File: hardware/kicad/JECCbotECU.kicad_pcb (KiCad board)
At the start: 2 copper layers, 100 x 60 mm, 70 parts, among them CN1 ADAFRUIT_FEATHER, CN2 691382010004, CN3 691382010005, CN4 691382010004, P1 USB_B, P2 CONN_02X05, P3 CONN_02X03, P4 CONN_02X05, P5 WR-TBL_691313710002, U1 STM32F103C8Tx, U2 BSS138, U3 BSS138, U4 BNO055, U5 TPS54335A, U6 GAPTEC_6S8W4_1.6RP, U7 LT1117, Y1 Crystal_Small

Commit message: bugfix
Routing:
- net +3V3: track 336.1 -> 330.5 mm
- net GND: vias 62 -> 63
- net +5V: vias 10 -> 7
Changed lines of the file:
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@@
     (thickness 1.6)
     (drawings 4)
-    (tracks 869)
+    (tracks 866)
     (zones 0)
     (modules 70)
@@
   (via (at 181.60492 61.33592) (size 0.8) (drill 0.4) (layers F.Cu B.Cu) (net 1))
   (via (at 142.70228 60.0964) (size 0.8) (drill 0.4) (layers F.Cu B.Cu) (net 1))
-  (via (at 147.39112 60.33008) (size 0.8) (drill 0.4) (layers F.Cu B.Cu) (net 1))
+  (via (at 146.66468 60.03544) (size 0.8) (drill 0.4) (layers F.Cu B.Cu) (net 1))
   (via (at 150.749 59.93892) (size 0.8) (drill 0.4) (layers F.Cu B.Cu) (net 1))
   (via (at 148.48332 43.84548) (size 0.8) (drill 0.4) (layers F.Cu B.Cu) (net 1))
@@
   (via (at 131.37388 47.36084) (size 0.8) (drill 0.4) (layers F.Cu B.Cu) (net 1))
   (via (at 128.40716 54.39156) (size 0.8) (drill 0.4) (layers F.Cu B.Cu) (net 1))
-  (via (at 144.10944 53.53304) (size 0.8) (drill 0.4) (layers F.Cu B.Cu) (net 1))
   (via (at 125.47092 55.03164) (size 0.8) (drill 0.4) (layers F.Cu B.Cu) (net 1))
   (via (at 130.28676 56.20512) (size 0.8) (drill 0.4) (layers F.Cu B.Cu) (net 1))
@@
   (via (at 151.11476 83.97748) (size 0.8) (drill 0.4) (layers F.Cu B.Cu) (net 1))
   (via (at 167.80256 86.97976) (size 0.8) (drill 0.4) (layers F.Cu B.Cu) (net 1))
+  (via (at 155.80868 57.72404) (size 0.8) (drill 0.4) (layers F.Cu B.Cu) (net 1))
+  (via (at 188.18352 46.66488) (size 0.8) (drill 0.4) (layers F.Cu B.Cu) (net 1))
   (segment (start 167.088 67.1) (end 165.64 67.1) (width 0.25) (layer F.Cu) (net 2))
   (segment (start 167.628 66.56) (end 167.088 67.1) (width 0.25) (layer F.Cu) (net 2))
@@
   (segment (start 169.4046 66.41916) (end 170.50512 65.31864) (width 1) (layer F.Cu) (net 2))
   (segment (start 170.53052 49.53508) (end 175.38592 49.54524) (width 1) (layer F.Cu) (net 2))
-  (segment (start 158.23 60.335) (end 157.42752 59.53252) (width 0.25) (layer F.Cu) (net 2))
-  (via (at 154.85364 59.5122) (size 0.8) (drill 0.4) (layers F.Cu B.Cu) (net 2))
-  (segment (start 157.42752 59.53252) (end 154.87396 59.53252) (width 0.25) (layer F.Cu) (net 2))
-  (segment (start 154.87396 59.53252) (end 154.85364 59.5122) (width 0.25) (layer F.Cu) (net 2))
-  (segment (start 155.419325 59.5122) (end 155.429485 59.50204) (width 0.25) (layer B.Cu) (net 2))
-  (segment (start 154.85364 59.5122) (end 155.419325 59.5122) (width 1) (layer B.Cu) (net 2))
-  (segment (start 155.429485 59.50204) (end 159.37484 59.50204) (width 1) (layer B.Cu) (net 2))
   (segment (start 159.37484 59.50204) (end 161.47288 57.404) (width 1) (layer B.Cu) (net 2))
   (segment (start 161.47288 57.404) (end 161.47288 56.0832) (width 1) (layer B.Cu) (net 2))
@@
   (segment (start 164.084 77.99) (end 165.0492 77.98816) (width 0.5) (layer F.Cu) (net 2))
   (segment (start 165.0492 77.98816) (end 166.70344 77.99) (width 0.5) (layer F.Cu) (net 2))
+  (segment (start 158.23 60.335) (end 158.23 60.32824) (width 0.25) (layer F.Cu) (net 2))
+  (via (at 157.61716 59.7154) (size 0.8) (drill 0.4) (layers F.Cu B.Cu) (net 2))
+  (segment (start 158.23 60.32824) (end 157.61716 59.7154) (width 0.25) (layer F.Cu) (net 2))
+  (segment (start 158.396205 59.50204) (end 159.37484 59.50204) (width 1) (layer B.Cu) (net 2))
+  (segment (start 158.182845 59.7154) (end 158.396205 59.50204) (width 1) (layer B.Cu) (net 2))
+  (segment (start 157.61716 59.7154) (end 158.182845 59.7154) (width 1) (layer B.Cu) (net 2))
   (segment (start 162.04 65.5) (end 162.04 60.96) (width 0.25) (layer F.Cu) (net 3))
   (segment (start 163.73094 58.211466) (end 163.73094 57.15) (width 0.25) (layer F.Cu) (net 3))
@@
   (segment (start 177.2666 46.4312) (end 177.30216 46.39564) (width 0.25) (layer B.Cu) (net 12))
   (segment (start 176.10836 46.39564) (end 177.292 46.39564) (width 1) (layer B.Cu) (net 12))
-  (via (at 154.813 53.21808) (size 0.8) (drill 0.4) (layers F.Cu B.Cu) (net 12))
-  (via (at 149.49932 56.1086) (size 0.8) (drill 0.4) (layers F.Cu B.Cu) (net 12))
-  (via (at 153.24836 56.73344) (size 0.8) (drill 0.4) (layers F.Cu B.Cu) (net 12))
   (via (at 142.20952 64.96812) (size 0.8) (drill 0.4) (layers F.Cu B.Cu) (net 13))
   (segment (start 142.20952 65.517882) (end 142.20952 64.96812) (width 0.25) (layer F.Cu) (net 13))
@@
   (segment (start 144.81048 47.95012) (end 145.4658 47.2948) (width 0.25) (layer F.Cu) (net 69))
   (zone (net 33) (net_name VBAT) (layer F.Cu) (hatch edge 0.508)
+    (priority 1)
     (connect_pads (clearance 0.508))
     (min_thickness 0.254)
@@
   )
   (zone (net 7) (net_name +12V) (layer F.Cu) (hatch edge 0.508)
+    (priority 1)
     (connect_pads (clearance 0.508))
     (min_thickness 0.254)
@@
   )
   (zone (net 11) (net_name /power/REG_5V_PH) (layer F.Cu) (hatch edge 0.508)
+    (priority 1)
     (connect_pads (clearance 0.508))
     (min_thickness 0.254)
@@
   )
   (zone (net 12) (net_name +5V) (layer F.Cu) (hatch edge 0.508)
+    (priority 1)
     (connect_pads (clearance 0.508))
     (min_thickness 0.254)
@@
     (polygon
       (pts
-        (xy 152.27808 52.50688) (xy 152.273 58.02376) (xy 151.60244 58.70956) (xy 144.62252 58.69432) (xy 144.02816 57.80024)
-        (xy 144.03832 52.21224) (xy 144.99336 51.83632) (xy 151.92756 51.83632)
-      )
-    )
-  )
-  (zone (net 12) (net_name +5V) (layer F.Cu) (hatch edge 0.508)
-    (connect_pads (clearance 0.508))
-    (min_thickness 0.254)
-    (fill yes (arc_segments 32) (thermal_gap 0.508) (thermal_bridge_width 0.508))
-    (polygon
-      (pts
-        (xy 157.26156 47.1932) (xy 157.38856 58.20664) (xy 156.6164 58.74512) (xy 151.384 58.74512) (xy 152.03932 53.15204)
-        (xy 151.82088 51.98364) (xy 151.83612 47.41164) (xy 152.33904 46.86808) (xy 153.20772 46.84776) (xy 156.8958 46.8122)
+        (xy 157.26156 47.1932) (xy 157.25648 53.9242) (xy 156.48432 54.46268) (xy 151.384 58.74512) (xy 151.388221 58.709092)
+        (xy 144.62252 58.69432) (xy 144.02816 57.80024) (xy 144.03832 52.21224) (xy 144.99336 51.83632) (xy 151.821371 51.83632)
+        (xy 151.83612 47.41164) (xy 152.33904 46.86808) (xy 153.20772 46.84776) (xy 156.8958 46.8122)
       )
     )
@@
       )
     )
+  )
+  (zone (net 1) (net_name GND) (layer B.Cu) (hatch edge 0.508)
+    (priority 1)
+    (connect_pads (clearance 0.508))
+    (min_thickness 0.254)
+    (fill yes (arc_segments 32) (thermal_gap 0.508) (thermal_bridge_width 0.508))
+    (polygon
+      (pts
+        (xy 189.96152 40.05072) (xy 190.02756 100.1776) (xy 89.87536 100.44176) (xy 89.97696 40.005)
+      )
+    )

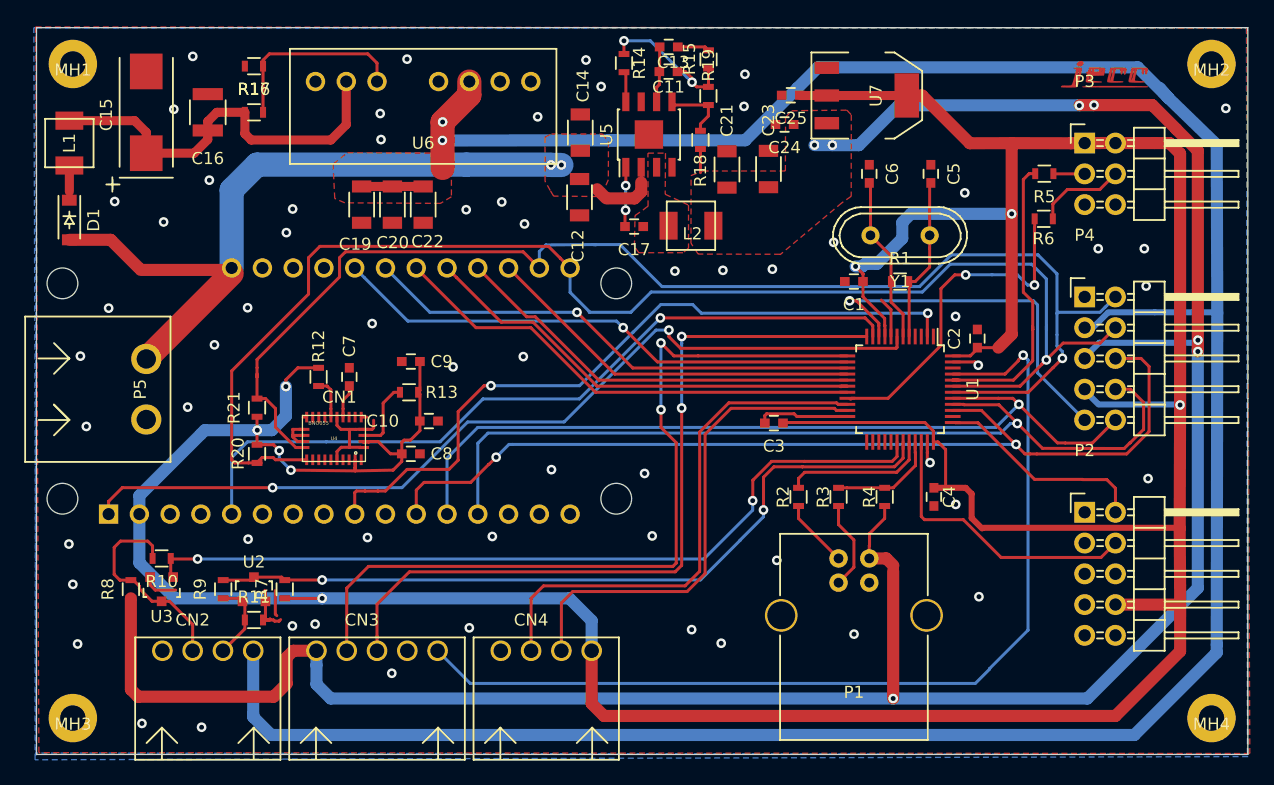
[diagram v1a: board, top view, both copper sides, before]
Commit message: silkscreen design
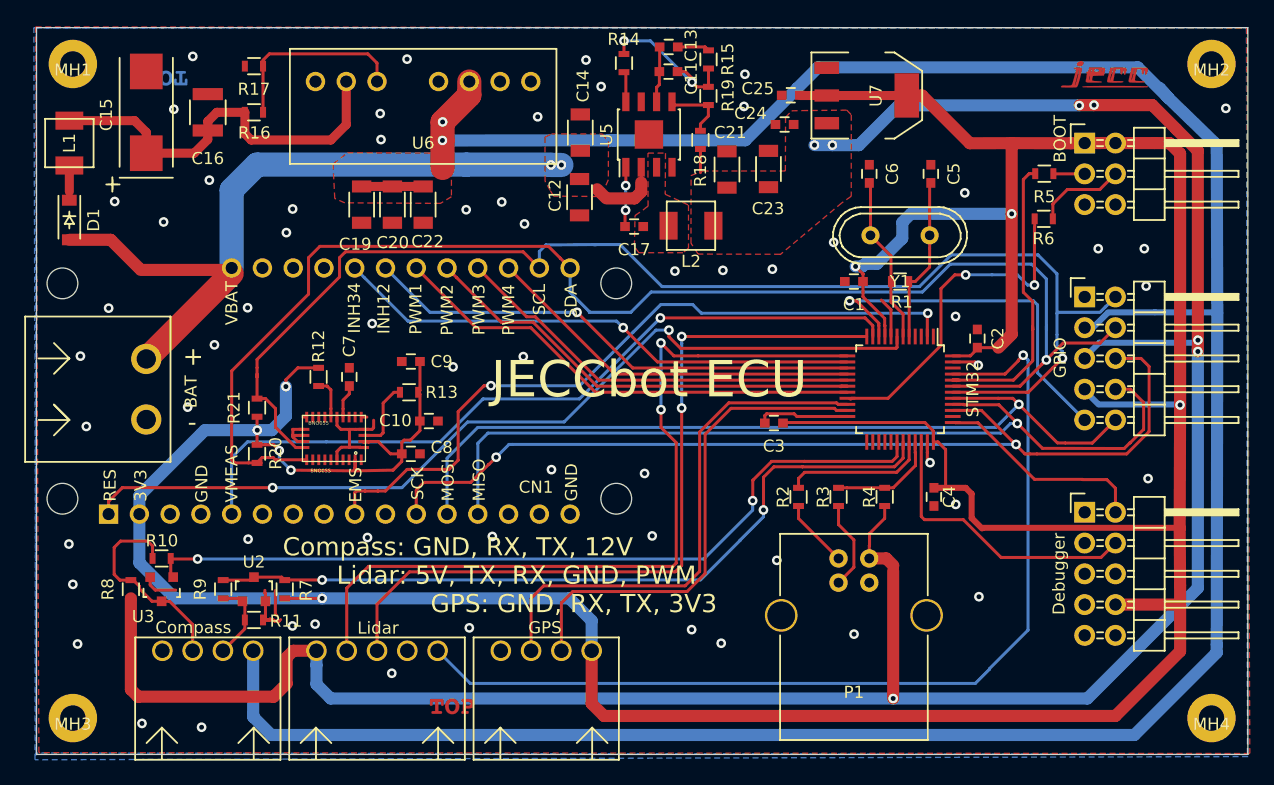
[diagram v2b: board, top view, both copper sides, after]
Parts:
- added G***: Label, labels:Bot, F.Cu at (100.7, 44.2)
- added G***: Label, labels:Top, F.Cu at (124.3, 96.0)
- renumbered P5 to BAT, U4 to BNO055, P3 to BOOT, CN2 to Compass, P2 to Debugger, P4 to GPIO, CN4 to GPS, CN3 to Lidar, U1 to STM32
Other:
- board text added: "+"
- board text added: "-"
- board text added: "3V3"
- board text added: "Compass: GND, RX, TX, 12V"
- board text added: "EMS"
- board text added: "GND"
- board text added: "GPS: GND, RX, TX, 3V3"
- board text added: "INH12"
- board text added: "INH34"
- board text added: "JECCbot ECU"
- board text added: "Lidar: 5V, TX, RX, GND, PWM"
- board text added: "MISO"
- board text added: "MOSI"
- board text added: "PWM1"
- board text added: "PWM2"
- board text added: "PWM3"
- board text added: "PWM4"
- board text added: "RES"
- board text added: "SCK"
- board text added: "SCL"
- board text added: "SDA"
- board text added: "VBAT"
- board text added: "VMEAS"

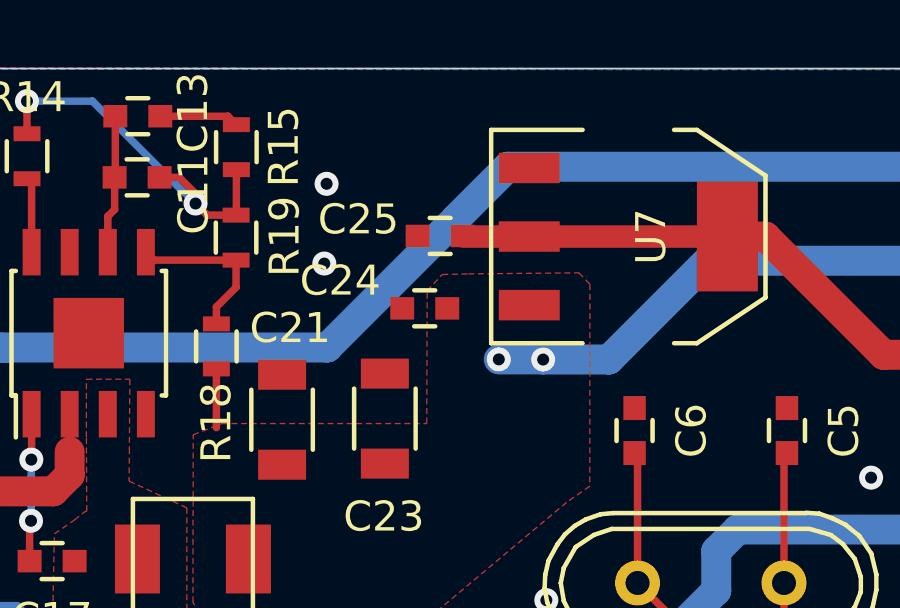
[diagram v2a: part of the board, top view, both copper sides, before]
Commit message: added silkscreen pinouts
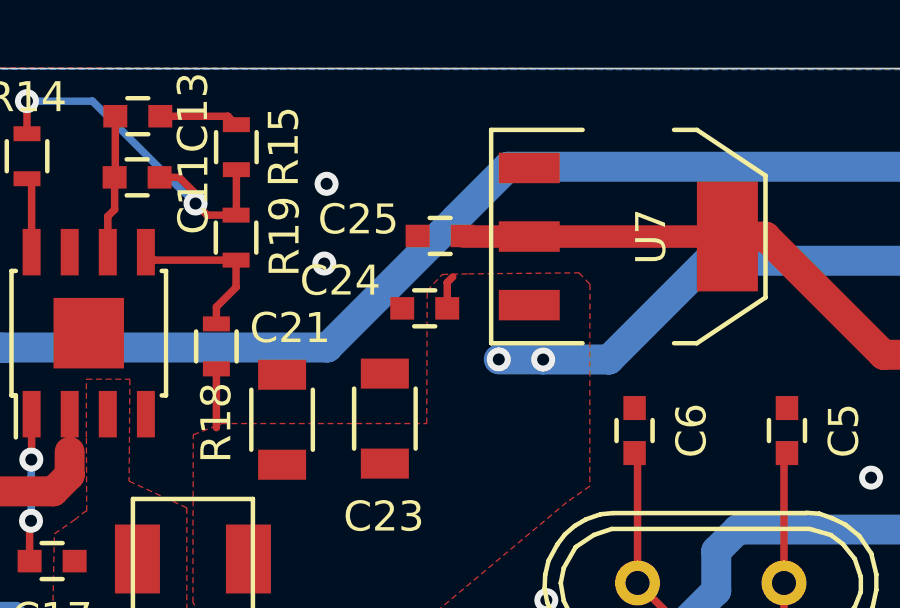
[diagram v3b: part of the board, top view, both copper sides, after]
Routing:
- net +5V: track 209.5 -> 210.6 mm
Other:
- board text added: "GPIO Header: 1: GND 2: SCL 3: 12V 4: SDA 5: 5V 6: SCK 7: 3V3 8: MISO 9: GPIO 10: MOSI"
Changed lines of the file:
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@@
   (general
     (thickness 1.6)
-    (drawings 28)
-    (tracks 866)
+    (drawings 29)
+    (tracks 868)
     (zones 0)
     (modules 72)
@@
     )
   )
+  (gr_text "GPIO Header: \n1: GND\n2: SCL\n3: 12V\n4: SDA\n5: 5V\n6: SCK\n7: 3V3\n8: MISO\n9: GPIO\n10: MOSI" (at 146.98472 69.27088) (layer B.SilkS)
+    (effects (font (size 1.5 1.5) (thickness 0.3)) (justify mirror))
+  )
   (gr_text "JECCbot ECU" (at 140.57376 69.04736) (layer F.SilkS)
     (effects (font (size 3 3) (thickness 0.3)))
@@
   (segment (start 177.2666 46.4312) (end 177.30216 46.39564) (width 0.25) (layer B.Cu) (net 12))
   (segment (start 176.10836 46.39564) (end 177.292 46.39564) (width 1) (layer B.Cu) (net 12))
+  (segment (start 152.50484 47.99584) (end 152.50484 47.13408) (width 0.25) (layer F.Cu) (net 12))
+  (segment (start 152.50484 47.13408) (end 152.68956 46.94936) (width 0.25) (layer F.Cu) (net 12))
   (via (at 142.20952 64.96812) (size 0.8) (drill 0.4) (layers F.Cu B.Cu) (net 13))
   (segment (start 142.20952 65.517882) (end 142.20952 64.96812) (width 0.25) (layer F.Cu) (net 13))

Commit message: finished layout
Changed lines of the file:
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@@
   (page A4)
   (layers
-    (0 F.Cu signal hide)
-    (31 B.Cu signal hide)
+    (0 F.Cu signal)
+    (31 B.Cu signal)
     (32 B.Adhes user)
     (33 F.Adhes user)
@@
     )
   )
-  (gr_text "GPIO Header: \n1: GND\n2: SCL\n3: 12V\n4: SDA\n5: 5V\n6: SCK\n7: 3V3\n8: MISO\n9: GPIO\n10: MOSI" (at 146.98472 69.27088) (layer B.SilkS)
+  (gr_text "GPIO Header: \n1: GND\n2: SCL\n3: 12V\n4: SDA\n5: 5V\n6: SCK\n7: 3V3\n8: MISO\n9: GPIO\n10: MOSI" (at 150.07844 65.69456 180) (layer B.SilkS)
     (effects (font (size 1.5 1.5) (thickness 0.3)) (justify mirror))
   )
@@
   (segment (start 144.74444 84.88172) (end 143.54048 86.08568) (width 0.25) (layer F.Cu) (net 41))
   (segment (start 92.71 53.54) (end 92.71 51.38) (width 0.75) (layer F.Cu) (net 42))
-  (segment (start 92.71 54.245) (end 92.71 53.54) (width 0.25) (layer F.Cu) (net 42))
+  (segment (start 92.71 53.54) (end 92.71 54.245) (width 0.75) (layer F.Cu) (net 42))
   (segment (start 156.21 85.81898) (end 157.48 84.54898) (width 0.25) (layer F.Cu) (net 43))
   (segment (start 157.48 84.54898) (end 157.48 82.296) (width 0.25) (layer F.Cu) (net 43))
